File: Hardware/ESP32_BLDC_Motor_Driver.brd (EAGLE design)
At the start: 100 x 80 mm, 67 parts, among them J2 0532610371, J3 POWER_JACKPOWER_JACK_SLOT, J6 0.1in header, Q1 20V/4.2A/52mΩ/1.4W, U1 TMC6300, U2 OPA344, U3 ESP-WROOM-3232D-NARROW, U4 CH340E_MSOP10, U6 AP63357

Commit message: Design Review Updates
Organized file folders, updates from design review - see document for full list of changes. Still needs a little more work before starting fully on the board file
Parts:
- removed R25: 18k, SparkFun-Resistors:0603
- added C10, C11: 22uF, SparkFun-Capacitors:0603
- added C12: 10uF, SparkFun-Capacitors:0603
- added C9: 0.1uF, SparkFun-Capacitors:0603
- added D2: WS2812_2020, SparkFun-LED:WS2812-2020
- added FRAME2: FRAME-LETTER, SparkFun-Aesthetics:CREATIVE_COMMONS
- added J7: QWIIC_RIGHT_ANGLE, SparkFun-Connectors:JST04_1MM_RA
- added J8: (no value), SparkFun-Connectors:1X02
- added L2: 4.7μH_SHIELDED_INDUCTOR, SparkFun-Coils:1008(2520)
- added LOGO4: QWIIC_LOGO_3MM, SparkFun-Aesthetics:QWIIC_3MM
- added Q2: (no value), SparkFun-DiscreteSemi:SC70-6
- added R16, R2, R3: 10k, SparkFun-Resistors:0603
- added R21: 20k, SparkFun-Resistors:0603
- added R22, R23: 100k, SparkFun-Resistors:0603
- added S2, S3, S4: MOMENTARY-SWITCH-SPST-SMD-4.6X2.8MM, SparkFun-Switches:TACTILE_SWITCH_SMD_4.6X2.8MM
- added TP1, TP10, TP11, TP2, TP3, TP4, TP5, TP6, TP7, TP8, TP9: TEST-POINT3X4, SparkFun-Connectors:PAD.03X.04
- added U5: ESD Diode, SparkFun-DiscreteSemi:SOT-23-6
- added U7: AP63203, SparkFun-IC-Power:SOT23-6
- C4: value 1nF -> 0.1uF
- R17, R4: value 10k -> 100k
- R20: value 2.0k -> 1.5k
- U4: value CH340E_MSOP10 -> CH340C; device SparkFun-IC-Comms:MSOP10 -> SparkFun-IC-Comms:SO016
- moved S1 170.3 mm to (-6.35, -141.0), turned to 0 degrees
- moved C4 159.7 mm to (-6.35, -130.8), turned to 0 degrees
- moved D4 159.0 mm to (-6.35, -105.4)
- moved R17 140.7 mm to (-6.35, -109.2), turned to 0 degrees
- moved R20 125.7 mm to (-2.54, -66.0)
- moved U4 123.7 mm to (1.27, -55.9), turned to 0 degrees
- moved R4 114.1 mm to (-2.54, -50.8)
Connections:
- net ESP_23 renamed ESP_23/PICO
- removed net N$24: S.2, U1.11
- removed net RESET: C4.1, R17.1, S1.3, S1.4, U3.3
- new net !RESET: Q2.4, R16.1, S2.3, S2.4, U3.3
- new net !STDBY: S.2, TP10.1, U1.11
- new net 3.3V_LDO: C10.1, C11.1, C3.1, C4.1, D2.VCC, J7.2, L2.2, R16.2, U2.5, U3.2, U7.1
- new net DTR: Q2.1, R2.2, U4.13
- new net EN: R17.1, U3.27, U6.P$2
- new net ESP_0/QPWR: Q2.6, S1.3, S1.4, TP1.1, U3.25
- new net ESP_19/POCI: U3.31
- new net ESP_21/TP_SDA: J7.3, U3.33
- new net ESP_22/TP_SCL: J7.4, U3.36
- new net ESP_34/AUX1: S4.1, S4.2, U3.6
- new net ESP_35/AUX2: S3.1, S3.2, U3.7
- new net N$10: C9.1, U7.6
- new net N$12: D2.DO, TP2.1
- new net N$13: C11.2
- new net N$2: R22.1, R23.2, U7.2
- new net N$7: Q2.5, R2.1
- new net N$8: Q2.2, R3.1
- new net N$9: C9.2, L2.1, U7.5
- new net RTS: Q2.3, R3.2, U4.14
- net 3.3V: now also U4.16, U4.4; no longer C3.1, R17.2, R4.2, U2.5, U3.2, U4.10, U4.7
- net CH340-RX: now also U4.3; no longer U4.9
- net CH340-TX: now also U4.2; no longer U4.8
- net CURR_SENSE: now also R21.2, TP11.1; no longer R25.2
- net D+: now also U4.5, U5.6; no longer U4.1
- net D-: now also U4.6, U5.4; no longer U4.2
- net DIAG: now also TP9.1
- net ESP_0: no longer U3.25
- net ESP_16: no longer U3.27
- net ESP_19: no longer U3.31
- net ESP_21: no longer U3.33
- net ESP_22: no longer U3.36
- net ESP_34: now also D2.DI; no longer U3.6
- net ESP_35: no longer U3.7
- net GND: now also C10.2, C12.2, D2.GND, J7.1, J8.1, R23.1, S2.1, S2.2, S3.3, S3.4, S4.3, S4.4, U4.1, U5.2, U7.4; no longer U4.3
- net N$28: now also D4.C; no longer D4.A
- net N$29: now also D4.A; no longer D4.C
- net N$6: now also R21.1; no longer R25.1
- net UH: now also TP3.1
- net UL: now also TP4.1
- net VH: now also TP5.1
- net VIN: now also C12.1, J8.2, R17.2, R22.2, R4.2, U7.3; no longer U6.P$2
- net VL: now also TP6.1
- net V_USB: now also U5.5
- net WH: now also TP7.1
- net WL: now also TP8.1

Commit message: Added datasheet, further changes from schematic review
See schematic review for more detailed changes: updated 3.3V LDO for an actual LDO, finished auto-reset circuitry, fixed pinout connections to breakout headers, changed size of logo, added qwiic logo, continued with layout. Datasheet added for the 3.3V LDO chosen.
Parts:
- removed C12: 10uF, SparkFun-Capacitors:0603
- removed FRAME2: FRAME-LETTER, SparkFun-Aesthetics:CREATIVE_COMMONS
- removed L2: 4.7μH_SHIELDED_INDUCTOR, SparkFun-Coils:1008(2520)
- removed LOGO1: SFE_LOGO_NAME.5_INCH, SparkFun-Aesthetics:SFE_LOGO_NAME_.5
- added LOGO5: SFE_LOGO_NAME.2_INCH, SparkFun-Aesthetics:SFE_LOGO_NAME_.2
- added R24: 100k, SparkFun-Resistors:0603
- C10: value 22uF -> 1.0uF
- C11: value 22uF -> 100pF
- C9: value 0.1uF -> 2.2uF
- R22: value 100k -> 16.2k
- R23: value 100k -> 26.7k
- U7: value AP63203 -> AP2202-ADJ; device SparkFun-IC-Power:SOT23-6 -> SparkFun-IC-Power:SOT23-5
- moved TP10 235.2 mm to (67.3, 22.9)
- moved TP11 230.2 mm to (61.0, 17.8)
- moved TP9 225.0 mm to (59.7, 17.8)
- moved J8 223.3 mm to (53.3, 57.1), turned to 90 degrees
- moved TP8 222.2 mm to (58.4, 17.8)
- moved TP7 217.3 mm to (52.1, 17.8)
- moved TP6 215.5 mm to (53.3, 17.8)
- moved TP5 214.8 mm to (57.1, 17.8)
- moved TP4 211.9 mm to (55.9, 17.8)
- moved TP3 209.1 mm to (54.6, 17.8)
- moved TP1 205.2 mm to (44.5, 44.5)
- moved LOGO4 201.7 mm to (71.1, 6.35)
- moved S1 188.6 mm to (44.5, 40.6), turned to 270 degrees
- moved TP2 186.3 mm to (25.4, 7.62)
- moved S4 185.2 mm to (30.5, 14.0), turned to 180 degrees
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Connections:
- net ESP_15 renamed ESP_15/GPIO4
- net ESP_16 renamed N$18
- net N$12 renamed TP2
- net N$16 renamed POWER_IN
- removed net ESP_0: J4.7
- removed net ESP_13: J4.5, U3.16
- removed net ESP_17: J5.2, U3.28
- removed net ESP_18: J5.4, U3.30
- removed net ESP_19: J5.5
- removed net ESP_2: J4.8, U3.24
- removed net ESP_21: J5.6
- removed net ESP_22: J5.7
- removed net ESP_34: D2.DI, J4.3
- removed net ESP_35: J4.4
- removed net ESP_36: J4.1, U3.4
- removed net ESP_39: J4.2, U3.5
- removed net N$10: C9.1, U7.6
- removed net N$13: C11.2
- removed net N$9: C9.2, L2.1, U7.5
- new net EN_MOTOR: R17.1, U3.27, U6.P$2
- new net ESP_12/GPIO1: J4.7, U3.14
- new net ESP_36/LED: D2.DI, J5.6, U3.4
- new net ESP_39/TP_A3: J5.5, U3.5
- new net ESP_4: J4.5, U3.26
- new net N$16: J5.2
- net !RESET: now also J5.3
- net !STDBY: now also U3.24
- net 3.3V_LDO: now also C9.1, R22.2, U7.5; no longer C10.1, C11.1, L2.2, U7.1
- net CURR_SENSE: now also J5.4
- net DIAG: now also U3.30; no longer U3.26
- net EN: now also R24.1, U3.28, U7.3; no longer R17.1, U3.27, U6.P$2
- net ESP_19/POCI: now also J4.4
- net ESP_21/TP_SDA: now also J4.2
- net ESP_22/TP_SCL: now also J4.1
- net ESP_23/PICO: now also J4.3; no longer J5.8
- net ESP_34/AUX1: now also J5.8
- net ESP_35/AUX2: now also J5.7
- net ESP_5: now also J4.8; no longer J5.3
- net GND: now also C11.2, C9.2, U7.2; no longer C12.2, U7.4
- net N$2: now also C11.1, U7.4; no longer U7.2
- net UH: now also U3.16; no longer U3.14
- net VIN: now also C10.1, R24.2, U7.1; no longer C12.1, R22.2, U7.3
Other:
- board size 100 x 80 mm -> 100 x 66 mm
- board text added: "v10"

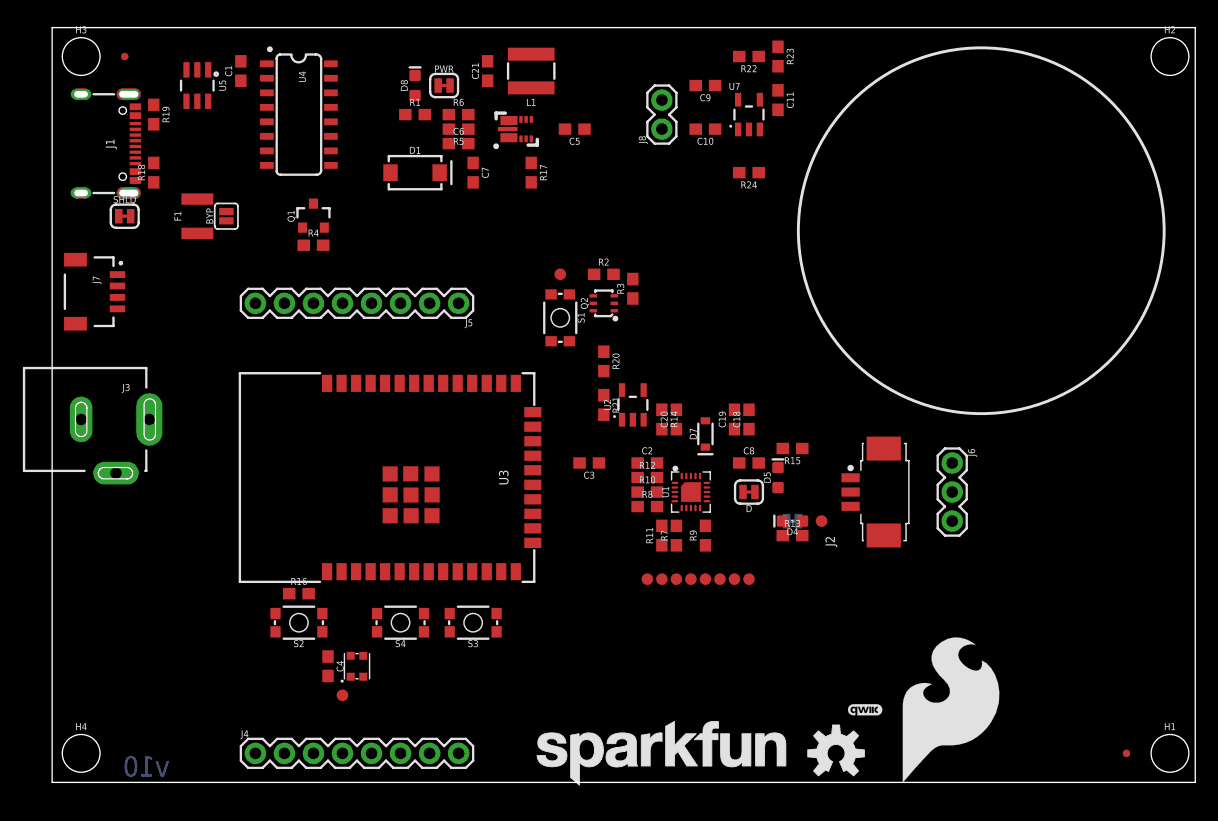
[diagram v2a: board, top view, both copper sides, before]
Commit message: Continue with design
Adjusted schematic components for better routing. Continued routing design - still a lot left to complete.
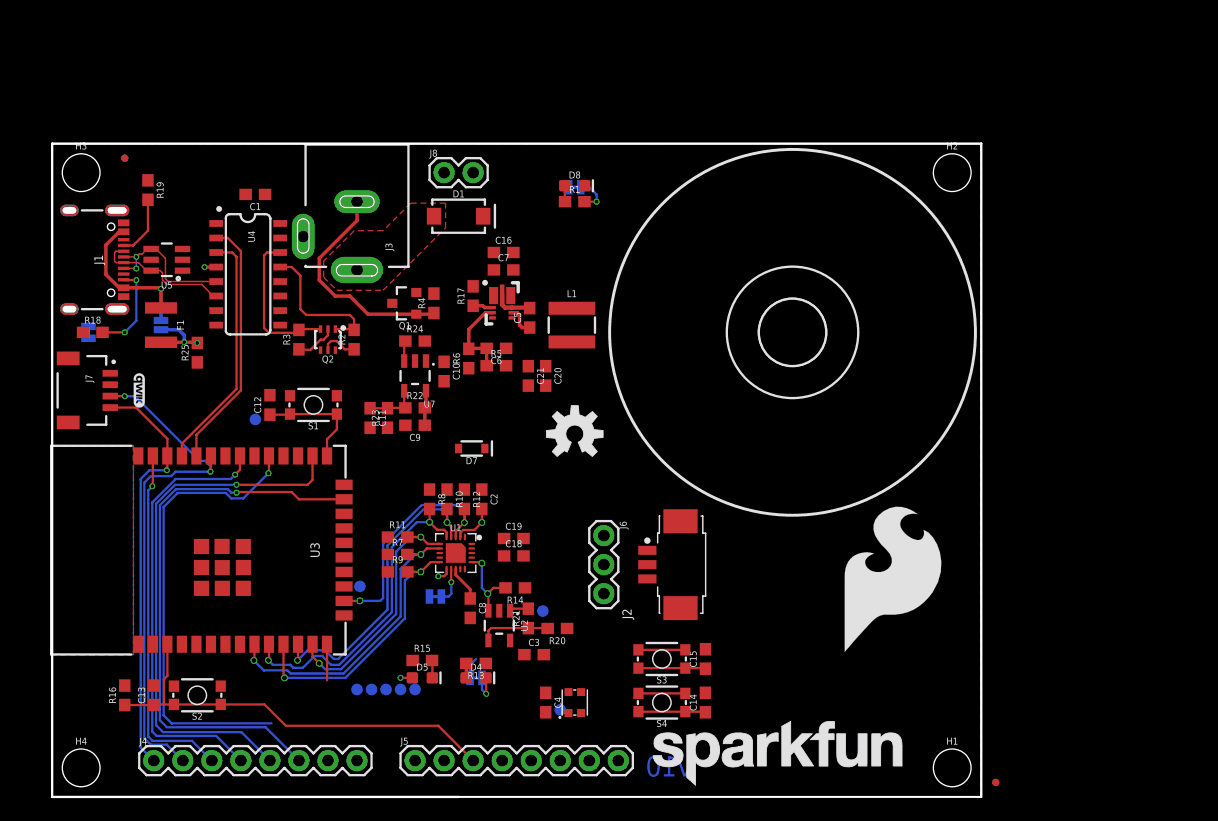
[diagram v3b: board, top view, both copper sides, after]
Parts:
- removed TP10, TP11: TEST-POINT3X4, SparkFun-Connectors:PAD.03X.04
- added C12, C13, C14, C15: 0.1uF, SparkFun-Capacitors:0603
- added C16: 10uF, SparkFun-Capacitors:0603
- added R25: 10k, SparkFun-Resistors:0603
- added U$1: (no value), SparkFun-Aesthetics:ORDERING_INSTRUCTIONS
- moved LOGO4 69.4 mm to (7.62, 34.3), turned to 270 degrees
- moved R23 46.6 mm to (29.3, 31.9), turned to 90 degrees
- moved C11 45.2 mm to (27.8, 31.9)
- moved R22 42.4 mm to (31.8, 32.8), turned to 0 degrees
- moved J5 40.2 mm to (31.8, 1.91), turned to 0 degrees
- moved C9 39.1 mm to (31.8, 31.2)
- moved R15 37.3 mm to (32.4, 10.7), turned to 0 degrees
- moved U7 37.1 mm to (31.8, 35.6), turned to 180 degrees
- moved LOGO2 36.1 mm to (45.7, 30.5)
- moved D5 35.7 mm to (32.4, 9.14), turned to 0 degrees
- moved TP8 33.2 mm to (26.7, 8.13), flipped to the bottom
- moved R24 32.7 mm to (31.8, 38.6), turned to 0 degrees
- moved C10 31.2 mm to (34.3, 35.9), turned to 270 degrees
- moved J6 31.1 mm to (48.3, 21.6)
- moved D4 30.9 mm to (37.1, 9.14), turned to 0 degrees
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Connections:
- net N$21 renamed BST
- net N$22 renamed SW
- net N$28 renamed S
- net N$30 renamed 1.8_VOUT
- net N$32 renamed D
- net N$36 renamed FB
- new net N$10: C14.1, S4.3, S4.4
- new net N$9: C15.1, S3.3, S3.4
- net !RESET: now also C13.1
- net !STDBY: no longer TP10.1
- net 3.3V: no longer C1.1, U4.16, U4.4
- net 3.3V_LDO: now also C1.1, U4.16, U4.4
- net CURR_SENSE: now also TP9.1; no longer TP11.1
- net D+: now also U5.4; no longer U5.6
- net D-: now also U5.6; no longer U5.4
- net DIAG: no longer TP9.1
- net ESP_0/QPWR: now also C12.1
- net GND: now also C12.2, C13.2, C14.2, C15.2, C16.2, R25.1; no longer S3.3, S3.4, S4.3, S4.4
- net VIN: now also C16.1
- net V_USB: now also R25.2
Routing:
- net ESP_15/GPIO4: track 0.00 -> 49.5 mm, vias 0 -> 1
- net ESP_4: track 0.00 -> 47.3 mm, vias 0 -> 1
- net ESP_21/TP_SDA: track 0.00 -> 45.9 mm, vias 0 -> 2
- net ESP_5: track 0.00 -> 40.3 mm, vias 0 -> 1
- net ESP_19/POCI: track 0.00 -> 38.9 mm, vias 0 -> 1
- net !RESET: track 0.00 -> 37.9 mm
- net ESP_22/TP_SCL: track 0.00 -> 36.6 mm, vias 0 -> 1
- net ESP_23/PICO: track 0.00 -> 31.2 mm, vias 0 -> 1
- net WH: track 0.00 -> 28.5 mm, vias 0 -> 2
- net VH: track 0.00 -> 27.4 mm, vias 0 -> 2
- net WL: track 0.00 -> 26.3 mm, vias 0 -> 2
- net VL: track 0.00 -> 23.9 mm, vias 0 -> 2
- net CH340-TX: track 0.00 -> 22.2 mm
- net UL: track 0.00 -> 22.1 mm, vias 0 -> 2
- net CH340-RX: track 0.00 -> 21.3 mm
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- added copper zone on layer 1, net GND
- added copper zone on layer 16, net GND
- added copper zone on layer 1, net POWER_IN
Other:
- board size 100 x 66 mm -> 81.3 x 57.2 mm
- board text added: "Board thickness is 1.6mm 4-Layer 1oz copper outer 1oz copper inner"
- board text added: "M. Chodikov"

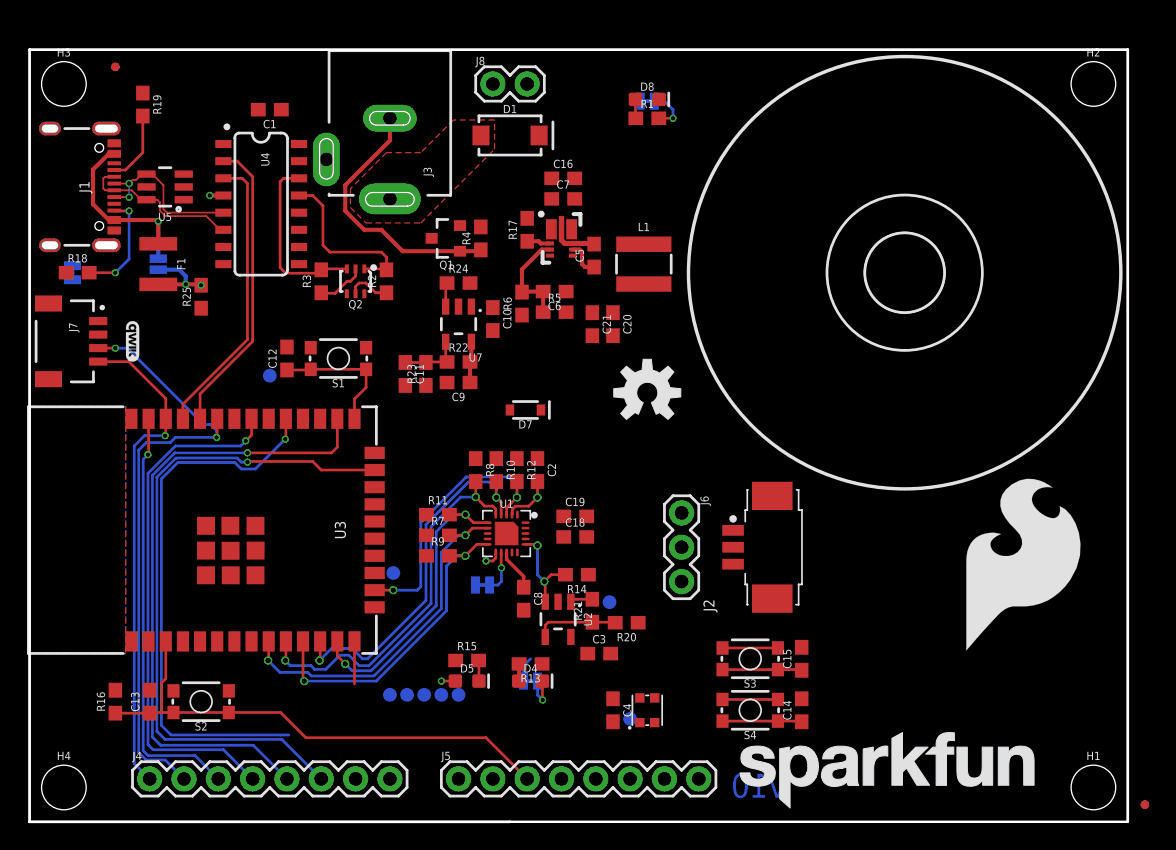
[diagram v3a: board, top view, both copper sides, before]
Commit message: Continued work on layout
Added polygons to layout, added layers 2,15, continued with routing
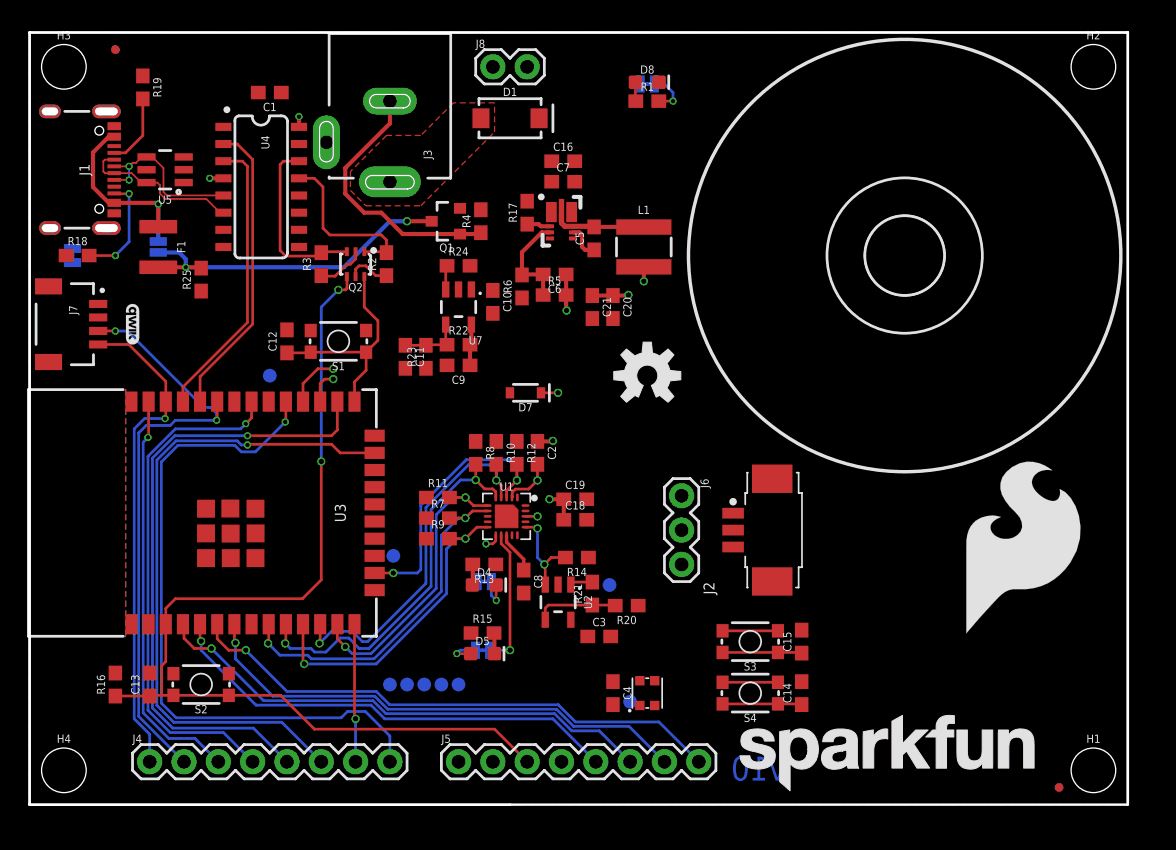
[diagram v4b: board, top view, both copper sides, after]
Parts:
- moved R13 8.13 mm to (33.7, 17.8)
- moved S 8.13 mm to (33.7, 16.5)
- moved D4 7.90 mm to (33.7, 16.3)
- moved FD1 6.48 mm to (76.2, 1.27)
- moved FD2 6.48 mm to (76.2, 1.27)
- moved D 4.83 mm to (33.5, 11.4)
- moved D5 2.33 mm to (33.5, 11.2)
- moved R15 2.33 mm to (33.5, 12.7)
- moved C16 1.27 mm to (39.5, 47.6)
- moved C19 1.27 mm to (40.4, 22.6)
- moved C6 1.27 mm to (38.9, 39.2)
- moved FD3 1.27 mm to (6.35, 55.9)
- moved FD4 1.27 mm to (6.35, 55.9)
- moved J1 1.27 mm to (6.60, 47.0)
- moved J3 1.27 mm to (26.7, 52.1)
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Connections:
- net U: now also J2.3, J6.3; no longer J2.1, J6.1
- net W: now also J2.1, J6.1; no longer J2.3, J6.3
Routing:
- net ESP_34/AUX1: track 4.10 -> 44.6 mm, vias 0 -> 1
- net ESP_36/LED: track 0.00 -> 37.9 mm, vias 0 -> 1
- net ESP_35/AUX2: track 4.10 -> 41.6 mm, vias 0 -> 1
- net !RESET: track 37.9 -> 75.0 mm, vias 0 -> 2
- net ESP_39/TP_A3: track 0.00 -> 34.6 mm, vias 0 -> 1
- net V_USB: track 6.04 -> 25.7 mm
- net 3.3V: track 0.00 -> 12.3 mm, vias 0 -> 7
- net ESP_5: track 40.3 -> 50.4 mm
- net DIAG: track 3.15 -> 10.3 mm
- net ESP_12/GPIO1: track 3.15 -> 10.2 mm, vias 0 -> 1
- net ESP_0/QPWR: track 9.90 -> 16.3 mm
- net EN: track 1.79 -> 5.82 mm, vias 0 -> 1
- net SW: track 3.45 -> 7.14 mm
- net EN_MOTOR: track 1.76 -> 4.20 mm, vias 0 -> 1
- net !STDBY: track 3.10 -> 1.23 mm
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- added copper zone on layer 15, net 3.3V
- added copper zone on layer 15, net 3.3V_LDO
- added copper zone on layer 2, net GND
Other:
- board size 81.3 x 57.2 mm -> 81.3 x 57.1 mm
